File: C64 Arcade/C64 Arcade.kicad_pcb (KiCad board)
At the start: 2 copper layers, 99.7 x 74.9 mm, 49 parts, among them J1 Port_1, J2 Port_2, M1 Mounting, M2 Mounting, M3 Mounting, M4 Mounting, Q1 2N3904, SW1 FIRE1, SW2 FIRE2, SW3 FIRE3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

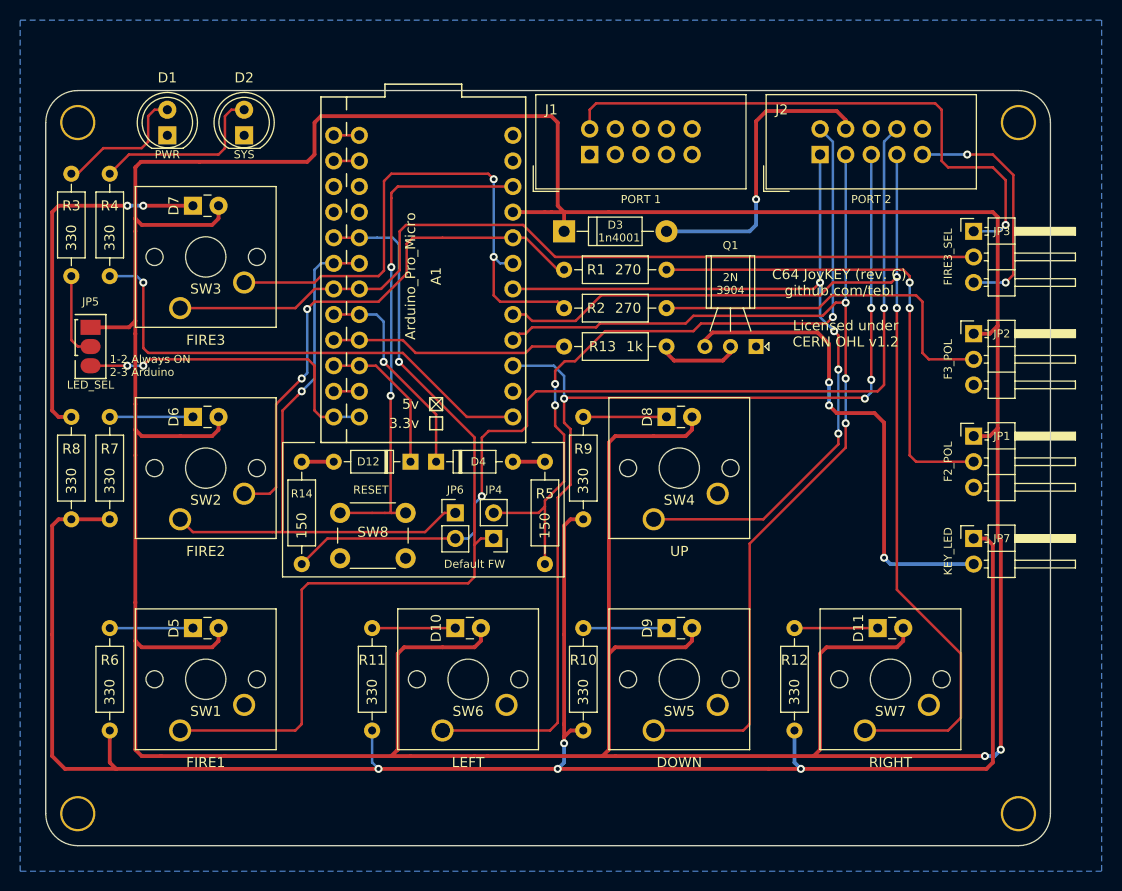
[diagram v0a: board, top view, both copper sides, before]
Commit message: Arcade board layout done
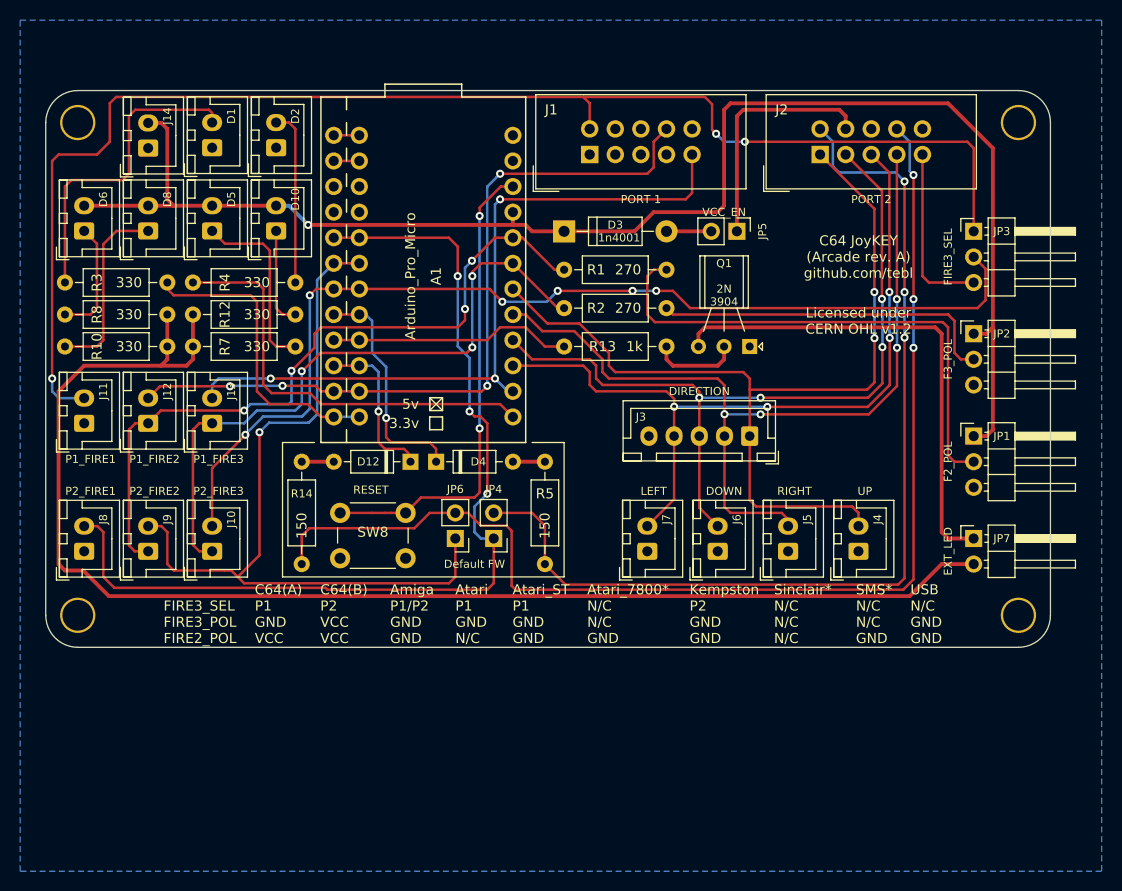
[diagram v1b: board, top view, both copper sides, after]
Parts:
- removed D11, D7, D9: LED, LED_THT:LED_Rectangular_W3.0mm_H2.0mm
- removed R11, R6, R9: 330, Resistor_THT:R_Axial_DIN0207_L6.3mm_D2.5mm_P10.16mm_Horizontal
- removed SW1: FIRE1, Button_Switch_Keyboard:SW_Cherry_MX_1.00u_PCB
- removed SW2: FIRE2, Button_Switch_Keyboard:SW_Cherry_MX_1.00u_PCB
- removed SW3: FIRE3, Button_Switch_Keyboard:SW_Cherry_MX_1.00u_PCB
- removed SW4: UP, Button_Switch_Keyboard:SW_Cherry_MX_1.00u_PCB
- removed SW5: DOWN, Button_Switch_Keyboard:SW_Cherry_MX_1.00u_PCB
- removed SW6: LEFT, Button_Switch_Keyboard:SW_Cherry_MX_1.00u_PCB
- removed SW7: RIGHT, Button_Switch_Keyboard:SW_Cherry_MX_1.00u_PCB
- added J10: P2_FIRE3, Connector_JST:JST_XH_B2B-XH-A_1x02_P2.50mm_Vertical, F.Cu at (157.5, 128.3)
- added J11: P1_FIRE1, Connector_JST:JST_XH_B2B-XH-A_1x02_P2.50mm_Vertical, F.Cu at (144.8, 115.6)
- added J12: P1_FIRE2, Connector_JST:JST_XH_B2B-XH-A_1x02_P2.50mm_Vertical, F.Cu at (151.1, 115.6)
- added J13: P1_FIRE3, Connector_JST:JST_XH_B2B-XH-A_1x02_P2.50mm_Vertical, F.Cu at (157.5, 115.6)
- added J14: EXT_PWR, Connector_JST:JST_XH_B2B-XH-A_1x02_P2.50mm_Vertical, F.Cu at (151.1, 88.3)
- added J3: DIRECTION, Connector_JST:JST_XH_B5B-XH-A_1x05_P2.50mm_Vertical, F.Cu at (210.8, 116.8)
- added J4: UP, Connector_JST:JST_XH_B2B-XH-A_1x02_P2.50mm_Vertical, F.Cu at (221.6, 128.3)
- added J5: RIGHT, Connector_JST:JST_XH_B2B-XH-A_1x02_P2.50mm_Vertical, F.Cu at (214.6, 128.3)
- added J6: DOWN, Connector_JST:JST_XH_B2B-XH-A_1x02_P2.50mm_Vertical, F.Cu at (207.6, 128.3)
- added J7: LEFT, Connector_JST:JST_XH_B2B-XH-A_1x02_P2.50mm_Vertical, F.Cu at (200.7, 128.3)
- added J8: P2_FIRE1, Connector_JST:JST_XH_B2B-XH-A_1x02_P2.50mm_Vertical, F.Cu at (144.8, 128.3)
- added J9: P2_FIRE2, Connector_JST:JST_XH_B2B-XH-A_1x02_P2.50mm_Vertical, F.Cu at (151.1, 128.3)
- D1, D2: footprint LEDs:LED_D5.0mm -> Connector_JST:JST_XH_B2B-XH-A_1x02_P2.50mm_Vertical
- D10, D5, D6, D8: value LED -> LED_Plugin; footprint LED_THT:LED_Rectangular_W3.0mm_H2.0mm -> Connector_JST:JST_XH_B2B-XH-A_1x02_P2.50mm_Vertical
- JP5: value LED_SEL -> VCC_EN; footprint solder_bridge:select -> Connector_PinHeader_2.54mm:PinHeader_1x02_P2.54mm_Vertical
- JP7: value KEY_LED -> EXT_LED
- moved R12 67.3 mm to (155.6, 104.8), turned to 0 degrees
- moved JP5 64.8 mm to (209.6, 96.5), turned to 270 degrees
- moved R10 58.5 mm to (142.9, 108.0), turned to 0 degrees
- moved D8 54.6 mm to (151.1, 96.5), turned to 90 degrees
- moved D10 43.2 mm to (163.8, 96.5), turned to 90 degrees
- moved D5 39.5 mm to (157.5, 96.5), turned to 90 degrees
- moved D6 21.4 mm to (144.8, 96.5), turned to 90 degrees
- moved R4 21.3 mm to (165.7, 101.6), turned to 180 degrees
- moved M1 19.7 mm to (144.1, 134.6)
- moved M2 19.7 mm to (237.5, 134.6)
- moved R7 10.8 mm to (155.6, 108.0), turned to 0 degrees
- moved R3 10.8 mm to (142.9, 101.6), turned to 0 degrees
- moved R8 10.2 mm to (142.9, 104.8), turned to 0 degrees
- moved D1 4.61 mm to (157.5, 88.2)
- moved D2 3.40 mm to (163.8, 88.2)
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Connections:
- net /FIRE1_OUT renamed /P2_FIRE1_OUT
- net /FIRE2_OUT renamed /P2_FIRE2_OUT
- net /UNDERGLOW renamed /EXT_LED
- A1 pad 11: Net-(A1-Pad11) -> P1_FIRE2
- A1 pad 14: (no net) -> P1_FIRE3
- J1 pad 5: (no net) -> P1_FIRE3
- J1 pad 9: (no net) -> P1_FIRE2
- J2 pad 7: Net-(D3-Pad2) -> Net-(J2-Pad7)
- JP5 pad 1: VCC -> Net-(J2-Pad7)
- JP5 pad 2: Net-(JP5-Pad2) -> Net-(D3-Pad2)
- Q1 pad 3: Net-(JP7-Pad2) -> Net-(JP7-Pad1)
- R10 pad 1: Net-(D9-Pad1) -> Net-(D8-Pad1)
- R10 pad 2: Net-(JP7-Pad1) -> Net-(JP7-Pad2)
- R12 pad 1: Net-(D11-Pad1) -> Net-(JP7-Pad2)
- R12 pad 2: Net-(JP7-Pad1) -> Net-(D10-Pad1)
- R3 pad 2: Net-(JP5-Pad2) -> /PWR
- R7 pad 1: Net-(D6-Pad1) -> Net-(JP7-Pad2)
- R7 pad 2: Net-(JP7-Pad1) -> Net-(D5-Pad1)
- R8 pad 1: Net-(D7-Pad1) -> Net-(D6-Pad1)
- R8 pad 2: Net-(JP7-Pad1) -> Net-(JP7-Pad2)
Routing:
- net VCC: track 436.0 -> 148.1 mm, vias 2 -> 1
- net Net-(JP7-Pad1): track 187.7 -> 49.0 mm, vias 4 -> 0
- net Net-(JP7-Pad2): track 48.6 -> 135.0 mm, vias 3 -> 0
- net P1_FIRE1: track 57.5 -> 137.9 mm, vias 1 -> 3
- net P1_FIRE2: track 0.00 -> 76.0 mm, vias 0 -> 4
- net P1_FIRE3: track 0.00 -> 73.7 mm, vias 0 -> 3
- net Net-(D7-Pad1): track 36.1 -> 0.00 mm, vias 2 -> 0
- net P2_LEFT: track 107.0 -> 77.8 mm
- net P2_DOWN: track 104.8 -> 79.1 mm, vias 3 -> 4
- net Net-(D3-Pad2): track 30.0 -> 4.44 mm, vias 1 -> 0
- net Net-(J2-Pad7): track 0.00 -> 24.0 mm
- net P2_RIGHT: track 108.8 -> 85.5 mm, vias 2 -> 4
- net P2_FIRE1: track 75.4 -> 98.2 mm
- net P2_FIRE2: track 97.6 -> 117.2 mm, vias 2 -> 3
- net Net-(D1-Pad2): track 13.6 -> 31.7 mm
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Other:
- board size 99.7 x 74.9 mm -> 99.7 x 55.2 mm
- board text added: "C64 JoyKEY (Arcade rev. A) github.com/tebl"
- board text added: "DIRECTION"
- board text added: "DOWN"
- board text added: "LED"
- board text added: "LEFT"
- board text added: "P1_FIRE1"
- board text added: "P1_FIRE2"
- board text added: "P1_FIRE3"
- board text added: "P2_FIRE1"
- board text added: "P2_FIRE2"
- board text added: "P2_FIRE3"
- board text added: "PWR"
- board text added: "RIGHT"
- board text added: "SYS"
- board text added: "UP"
- board text removed: "1-2 Always ON 2-3 Arduino"
- board text removed: "C64 JoyKEY (rev. C) github.com/tebl"
- board text removed: "~IMPORTANT! Configure FIRE2/FIRE3 polarity according to what the system required by the system, leave unjumpered (N/C) if you are not sure. You break it, you fix it!"

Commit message: Added UP_EN for direction
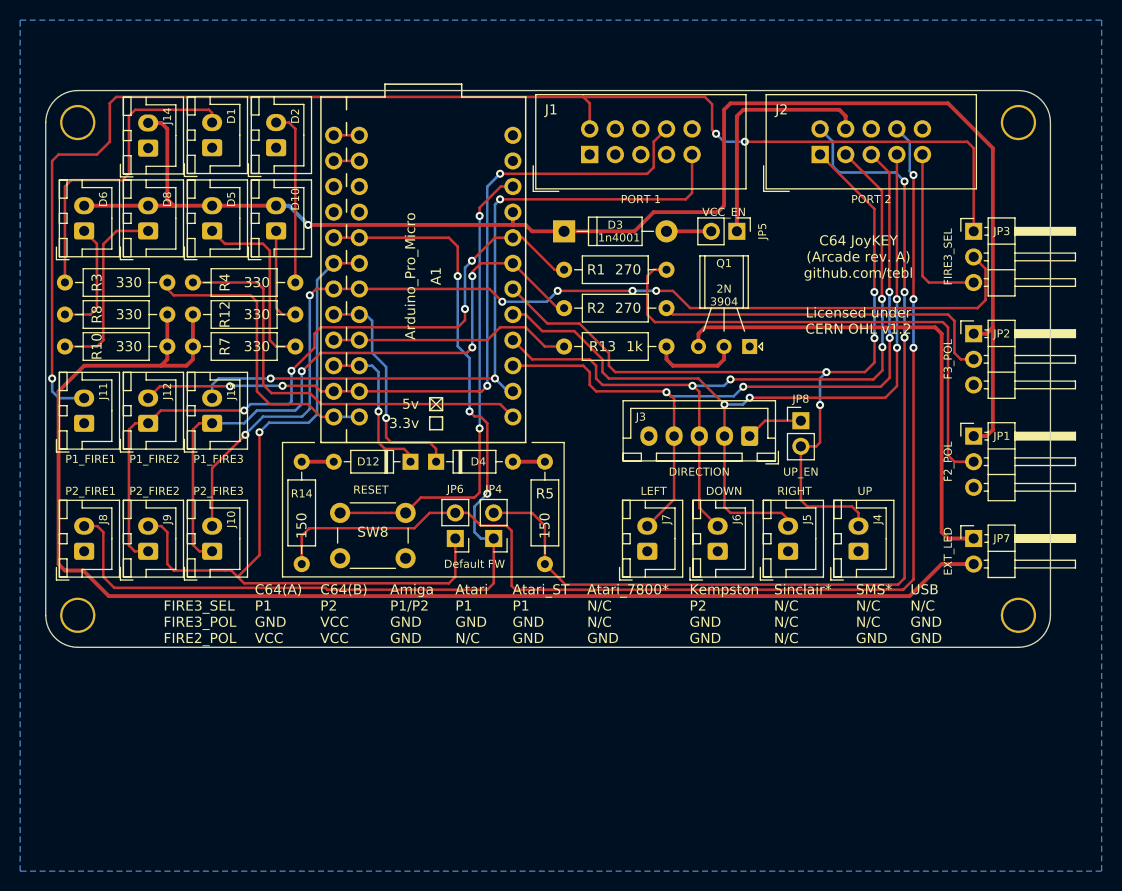
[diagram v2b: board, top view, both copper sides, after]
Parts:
- added JP8: UP_EN, Connector_PinHeader_2.54mm:PinHeader_1x02_P2.54mm_Vertical, F.Cu at (215.9, 115.3)
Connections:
- J3 pad 1: P2_UP -> Net-(J3-Pad1)
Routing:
- net Net-(J3-Pad1): track 0.00 -> 5.71 mm
- net P2_UP: track 90.1 -> 85.5 mm, vias 2 -> 4
- net P2_RIGHT: track 85.5 -> 84.0 mm
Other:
- board text added: "UP_EN"
- board text added: "VCC_EN"

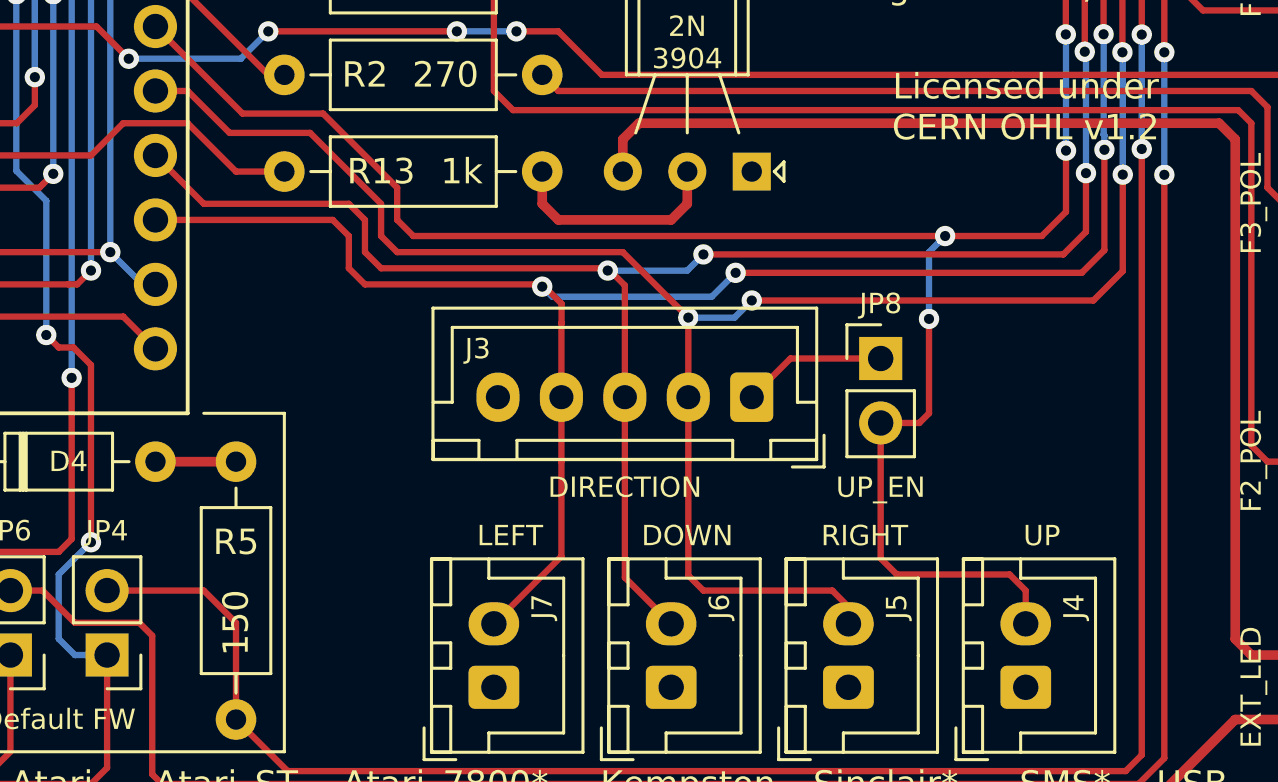
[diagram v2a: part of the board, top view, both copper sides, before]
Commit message: Fixed Arcade pinout and added isolation for Arduino (need new layout)
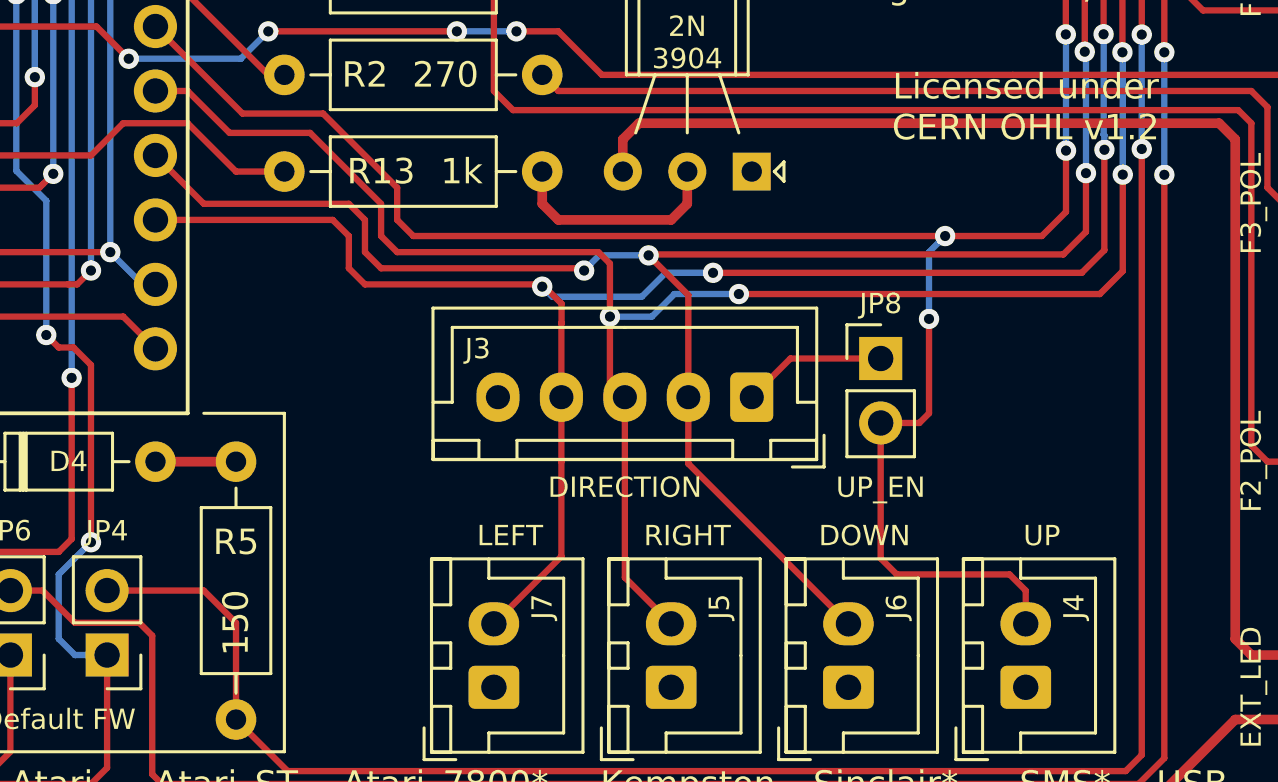
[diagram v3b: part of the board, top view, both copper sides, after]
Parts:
- moved J5 6.98 mm to (207.6, 128.3)
- moved J6 6.98 mm to (214.6, 128.3)
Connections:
- J3 pad 2: P2_RIGHT -> P2_DOWN
- J3 pad 3: P2_DOWN -> P2_RIGHT
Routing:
- net P2_RIGHT: track 84.0 -> 80.6 mm
- net P2_DOWN: track 78.6 -> 81.3 mm
